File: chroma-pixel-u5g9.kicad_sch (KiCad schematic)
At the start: 0 parts

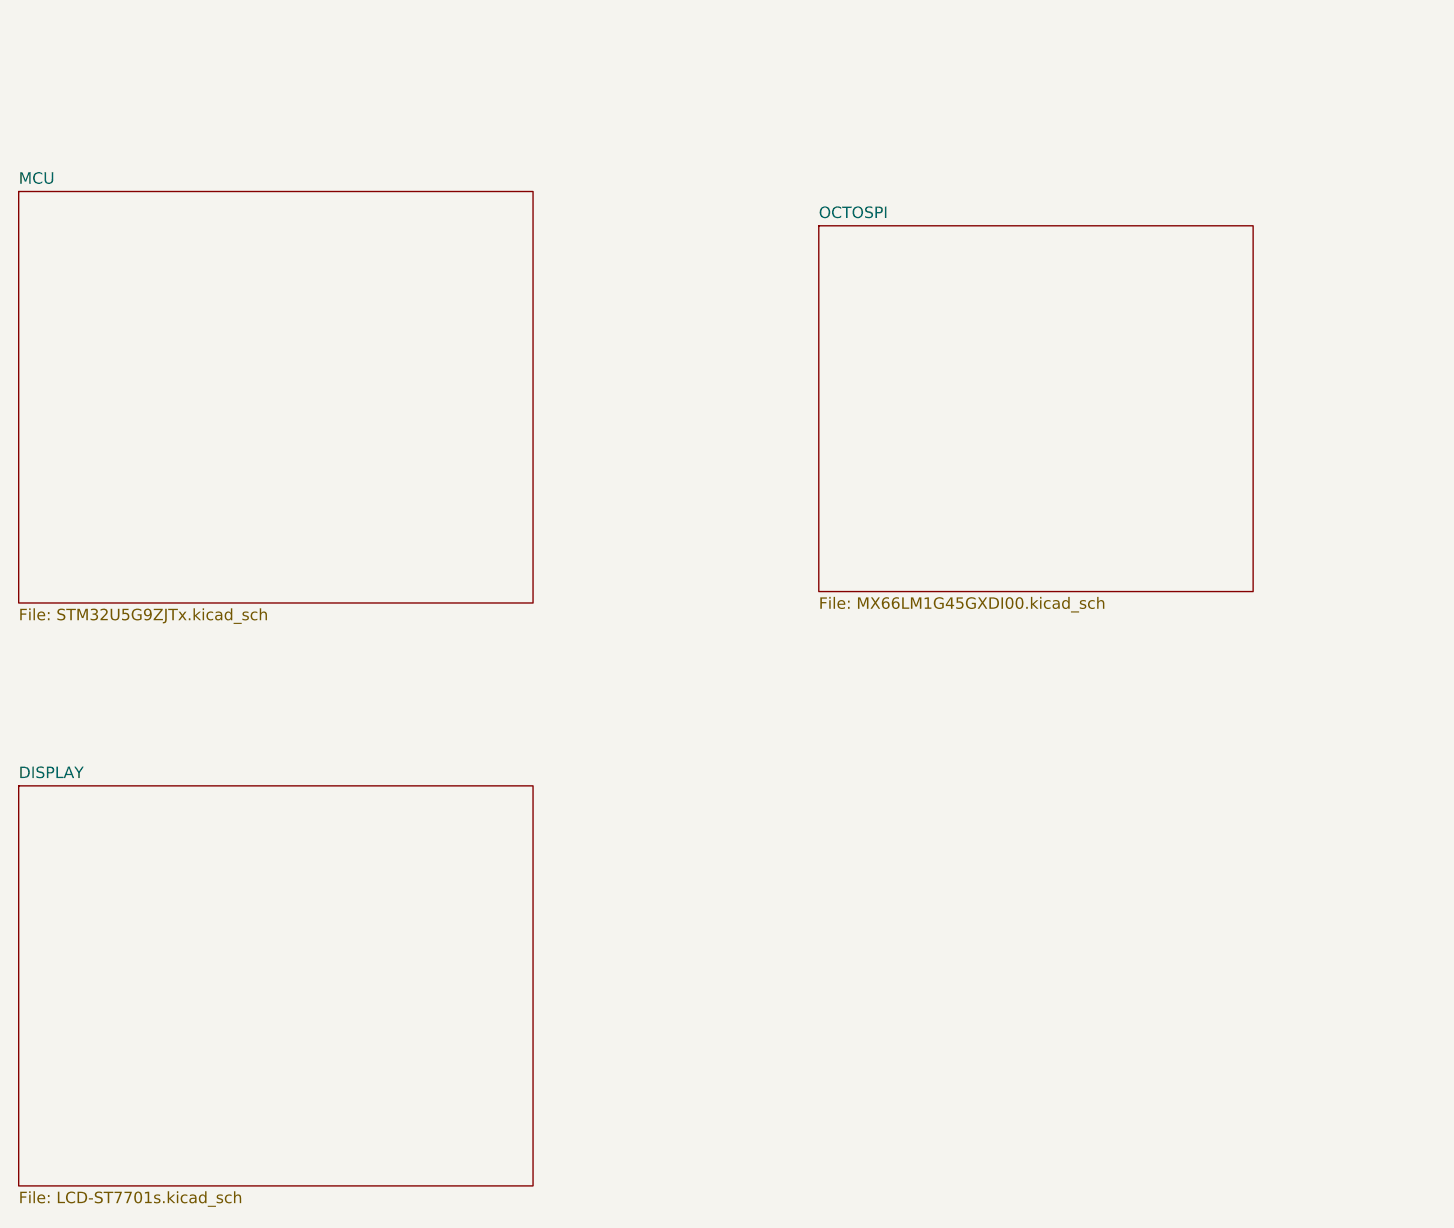
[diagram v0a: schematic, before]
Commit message: Added Battery Fuel Gauge, Battery Charger and 5V boost voltage
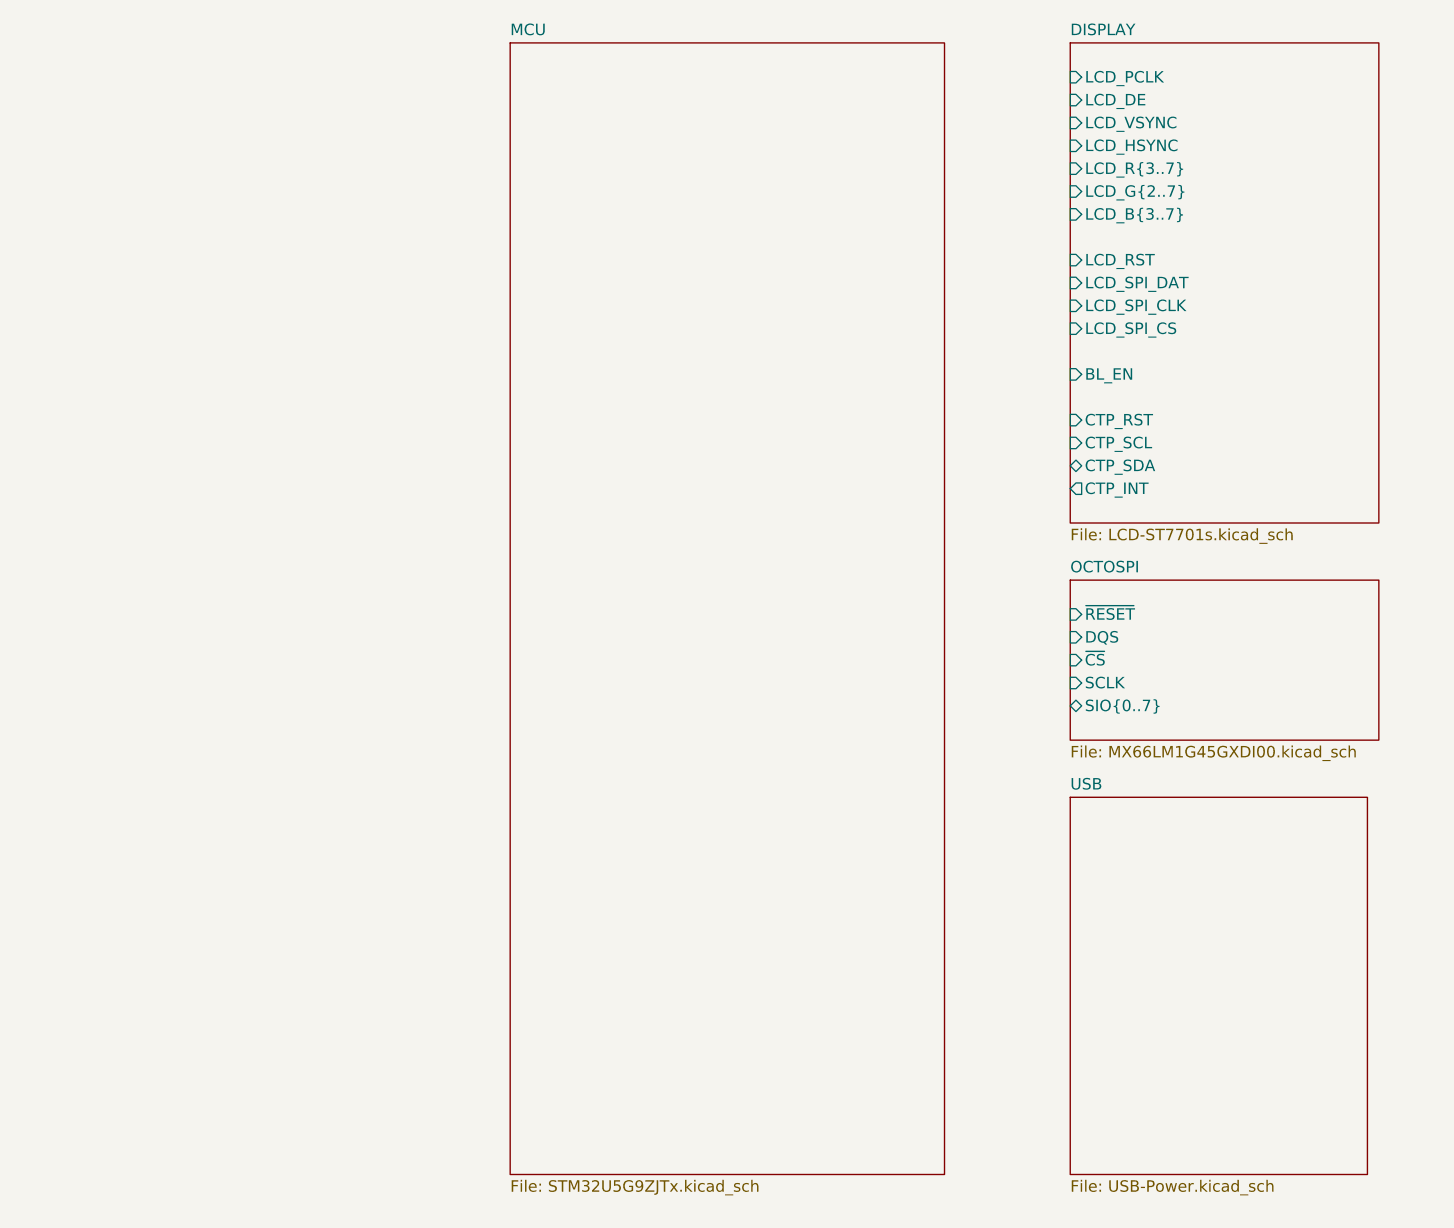
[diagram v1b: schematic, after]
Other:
- added sheet USB (USB-Power.kicad_sch)
- sheet DISPLAY ports: added BL_EN, CTP_INT, CTP_RST, CTP_SCL, CTP_SDA, LCD_B{3..7}, LCD_DE, LCD_G{2..7}, LCD_HSYNC, LCD_PCLK, LCD_RST, LCD_R{3..7}, LCD_SPI_CLK, LCD_SPI_CS, LCD_SPI_DAT, LCD_VSYNC; removed none
- sheet OCTOSPI ports: added DQS, SCLK, SIO{0..7}, ~{CS}, ~{RESET}; removed none

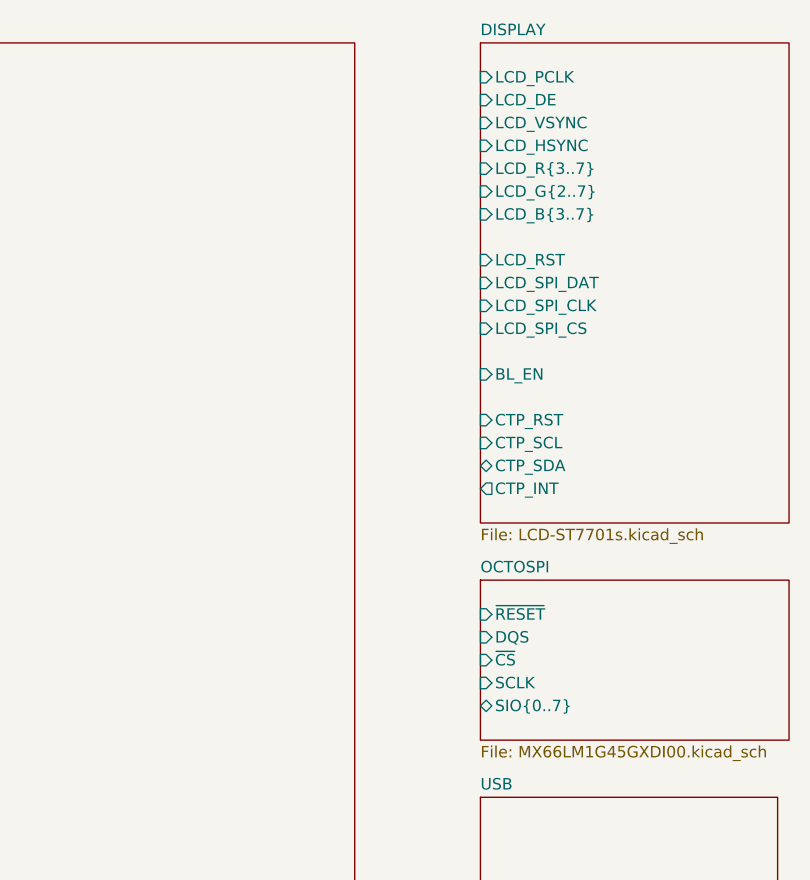
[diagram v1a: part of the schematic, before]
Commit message: Add connection from OSPI Flash and LCD to MCU
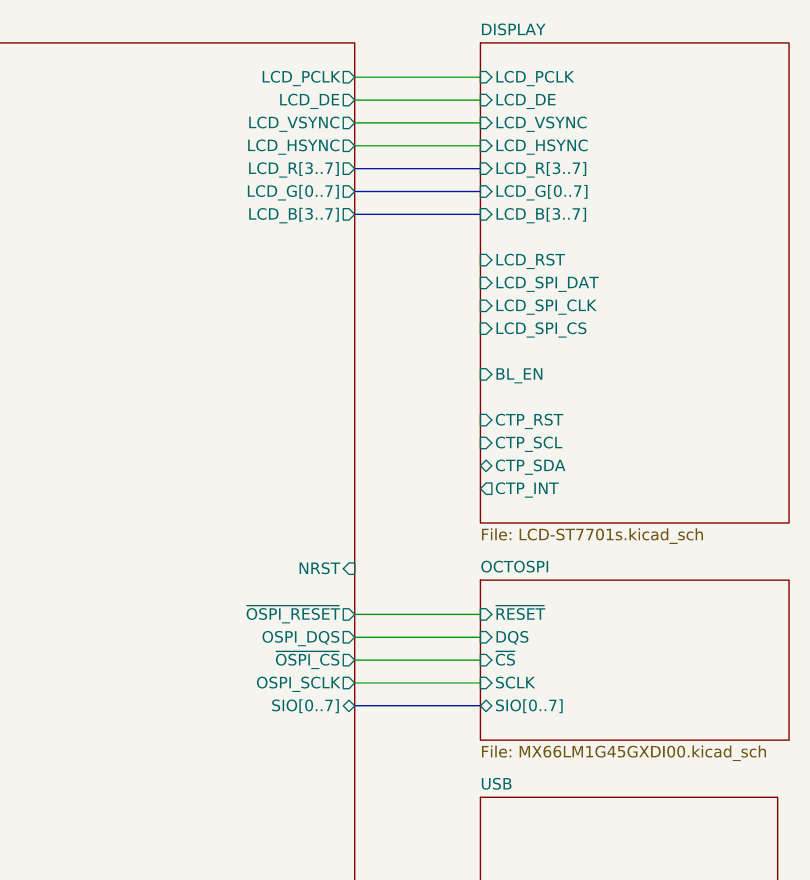
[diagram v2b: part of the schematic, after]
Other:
- sheet DISPLAY ports: added LCD_B[3..7], LCD_G[0..7], LCD_R[3..7]; removed LCD_B{3..7}, LCD_G{2..7}, LCD_R{3..7}
- sheet MCU ports: added LCD_B[3..7], LCD_DE, LCD_G[0..7], LCD_HSYNC, LCD_PCLK, LCD_R[3..7], LCD_VSYNC, NRST, OSPI_DQS, OSPI_SCLK, SIO[0..7], ~{OSPI_CS}, ~{OSPI_RESET}; removed none
- sheet OCTOSPI ports: added SIO[0..7]; removed SIO{0..7}
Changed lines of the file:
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@@
 	(generator_version "9.0")
 	(paper "A4")
+	(bus
+		(pts
+			(xy 147.32 101.6) (xy 161.29 101.6)
+		)
+		(stroke
+			(width 0)
+			(type default)
+		)
+	)
+	(wire
+		(pts
+			(xy 147.32 99.06) (xy 161.29 99.06)
+		)
+		(stroke
+			(width 0)
+			(type default)
+		)
+	)
+	(wire
+		(pts
+			(xy 147.32 31.75) (xy 161.29 31.75)
+		)
+		(stroke
+			(width 0)
+			(type default)
+		)
+	)
+	(wire
+		(pts
+			(xy 147.32 34.29) (xy 161.29 34.29)
+		)
+		(stroke
+			(width 0)
+			(type default)
+		)
+	)
+	(bus
+		(pts
+			(xy 147.32 46.99) (xy 161.29 46.99)
+		)
+		(stroke
+			(width 0)
+			(type default)
+		)
+	)
+	(bus
+		(pts
+			(xy 147.32 41.91) (xy 161.29 41.91)
+		)
+		(stroke
+			(width 0)
+			(type default)
+		)
+	)
+	(bus
+		(pts
+			(xy 147.32 44.45) (xy 161.29 44.45)
+		)
+		(stroke
+			(width 0)
+			(type default)
+		)
+	)
+	(wire
+		(pts
+			(xy 147.32 93.98) (xy 161.29 93.98)
+		)
+		(stroke
+			(width 0)
+			(type default)
+		)
+	)
+	(wire
+		(pts
+			(xy 147.32 91.44) (xy 161.29 91.44)
+		)
+		(stroke
+			(width 0)
+			(type default)
+		)
+	)
+	(wire
+		(pts
+			(xy 147.32 96.52) (xy 161.29 96.52)
+		)
+		(stroke
+			(width 0)
+			(type default)
+		)
+	)
+	(wire
+		(pts
+			(xy 147.32 36.83) (xy 161.29 36.83)
+		)
+		(stroke
+			(width 0)
+			(type default)
+		)
+	)
+	(wire
+		(pts
+			(xy 147.32 39.37) (xy 161.29 39.37)
+		)
+		(stroke
+			(width 0)
+			(type default)
+		)
+	)
 	(sheet
 		(at 161.29 111.76)
@@
 			)
 		)
+		(pin "NRST" input
+			(at 147.32 86.36 0)
+			(effects
+				(font
+					(size 1.27 1.27)
+				)
+				(justify right)
+			)
+		)
+		(pin "OSPI_SCLK" output
+			(at 147.32 99.06 0)
+			(effects
+				(font
+					(size 1.27 1.27)
+				)
+				(justify right)
+			)
+		)
+		(pin "~{OSPI_RESET}" output
+			(at 147.32 91.44 0)
+			(effects
+				(font
+					(size 1.27 1.27)
+				)
+				(justify right)
+			)
+		)
+		(pin "OSPI_DQS" output
+			(at 147.32 93.98 0)
+			(effects
+				(font
+					(size 1.27 1.27)
+				)
+				(justify right)
+			)
+		)
+		(pin "~{OSPI_CS}" output
+			(at 147.32 96.52 0)
+			(effects
+				(font
+					(size 1.27 1.27)
+				)
+				(justify right)
+			)
+		)
+		(pin "SIO[0..7]" bidirectional
+			(at 147.32 101.6 0)
+			(effects
+				(font
+					(size 1.27 1.27)
+				)
+				(justify right)
+			)
+		)
+		(pin "LCD_R[3..7]" output
+			(at 147.32 41.91 0)
+			(effects
+				(font
+					(size 1.27 1.27)
+				)
+				(justify right)
+			)
+		)
+		(pin "LCD_B[3..7]" output
+			(at 147.32 46.99 0)
+			(effects
+				(font
+					(size 1.27 1.27)
+				)
+				(justify right)
+			)
+		)
+		(pin "LCD_PCLK" output
+			(at 147.32 31.75 0)
+			(effects
+				(font
+					(size 1.27 1.27)
+				)
+				(justify right)
+			)
+		)
+		(pin "LCD_G[0..7]" output
+			(at 147.32 44.45 0)
+			(effects
+				(font
+					(size 1.27 1.27)
+				)
+				(justify right)
+			)
+		)
+		(pin "LCD_DE" output
+			(at 147.32 34.29 0)
+			(effects
+				(font
+					(size 1.27 1.27)
+				)
+				(justify right)
+			)
+		)
+		(pin "LCD_VSYNC" output
+			(at 147.32 36.83 0)
+			(effects
+				(font
+					(size 1.27 1.27)
+				)
+				(justify right)
+			)
+		)
+		(pin "LCD_HSYNC" output
+			(at 147.32 39.37 0)
+			(effects
+				(font
+					(size 1.27 1.27)
+				)
+				(justify right)
+			)
+		)
 		(instances
 			(project "chroma-pixel-u5g9"
@@
 			)
 		)
-		(pin "LCD_R{3..7}" input
-			(at 161.29 41.91 180)
-			(effects
-				(font
-					(size 1.27 1.27)
-				)
-				(justify left)
-			)
-		)
 		(pin "CTP_SDA" bidirectional
 			(at 161.29 74.93 180)
@@
 			)
 		)
-		(pin "LCD_G{2..7}" input
+		(pin "LCD_B[3..7]" input
+			(at 161.29 46.99 180)
+			(effects
+				(font
+					(size 1.27 1.27)
+				)
+				(justify left)
+			)
+		)
+		(pin "LCD_G[0..7]" input
 			(at 161.29 44.45 180)
 			(effects
@@
 			)
 		)
-		(pin "LCD_B{3..7}" input
-			(at 161.29 46.99 180)
+		(pin "LCD_R[3..7]" input
+			(at 161.29 41.91 180)
 			(effects
 				(font
@@
 			)
 		)
-		(pin "SIO{0..7}" bidirectional
-			(at 161.29 101.6 180)
-			(effects
-				(font
-					(size 1.27 1.27)
-				)
-				(justify left)
-			)
-		)
 		(pin "DQS" input
 			(at 161.29 93.98 180)
 			(effects
 				(font
+					(size 1.27 1.27)
+				)
+				(justify left)
+			)
+		)
+		(pin "SIO[0..7]" bidirectional
+			(at 161.29 101.6 180)
+			(effects
+				(font
